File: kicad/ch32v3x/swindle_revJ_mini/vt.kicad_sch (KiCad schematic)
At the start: 8 parts, among them J2 Conn_01x03_Socket, U3 3V->VTREF, U4 VTREF->3V, U5 VTREF<->3V, U6 RT9013-33GB

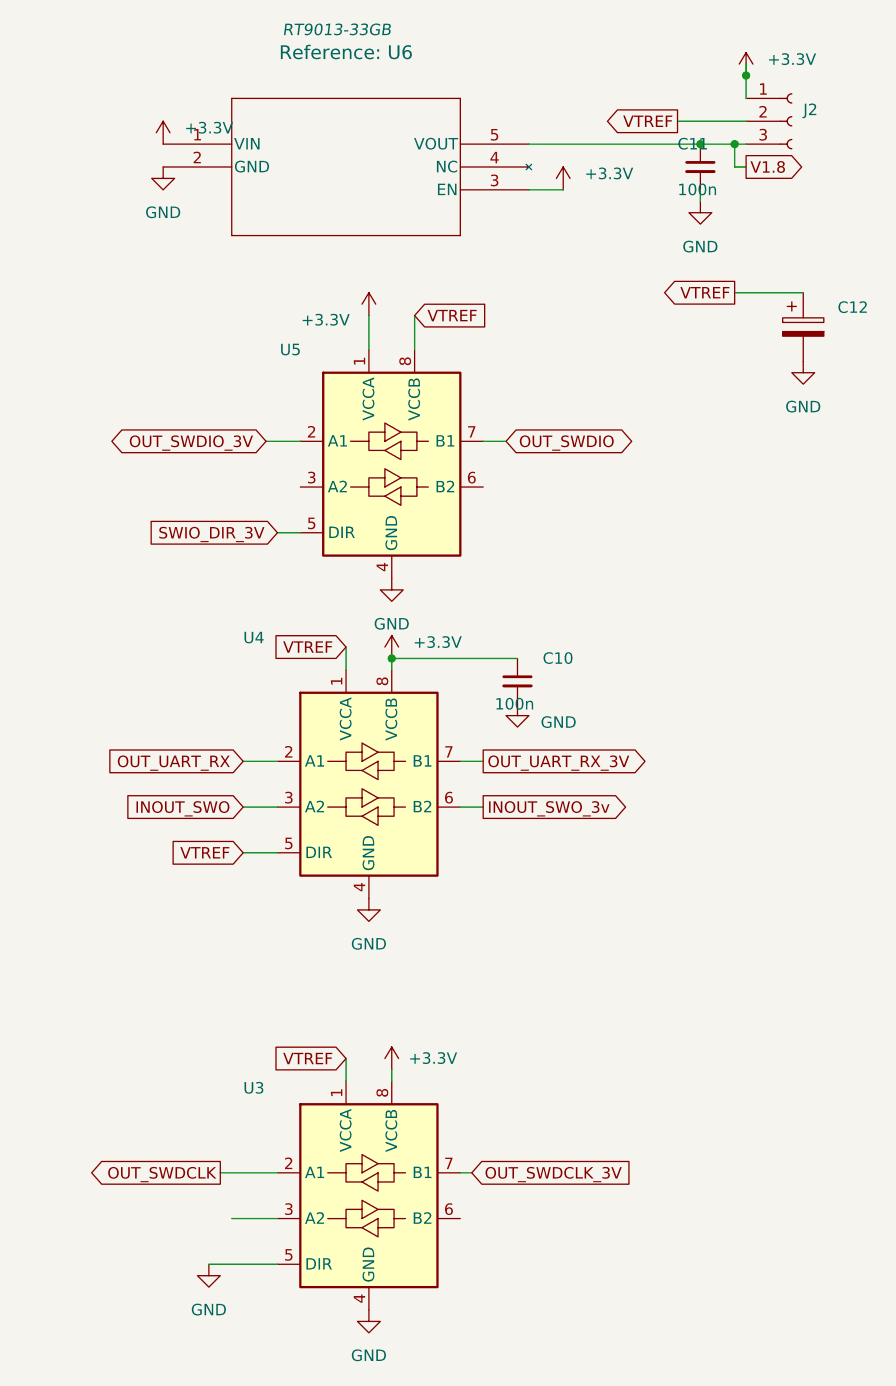
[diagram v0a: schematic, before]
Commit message: add a WS2812b to the mini version, mini version for CH32,GD32 and RP2xxx
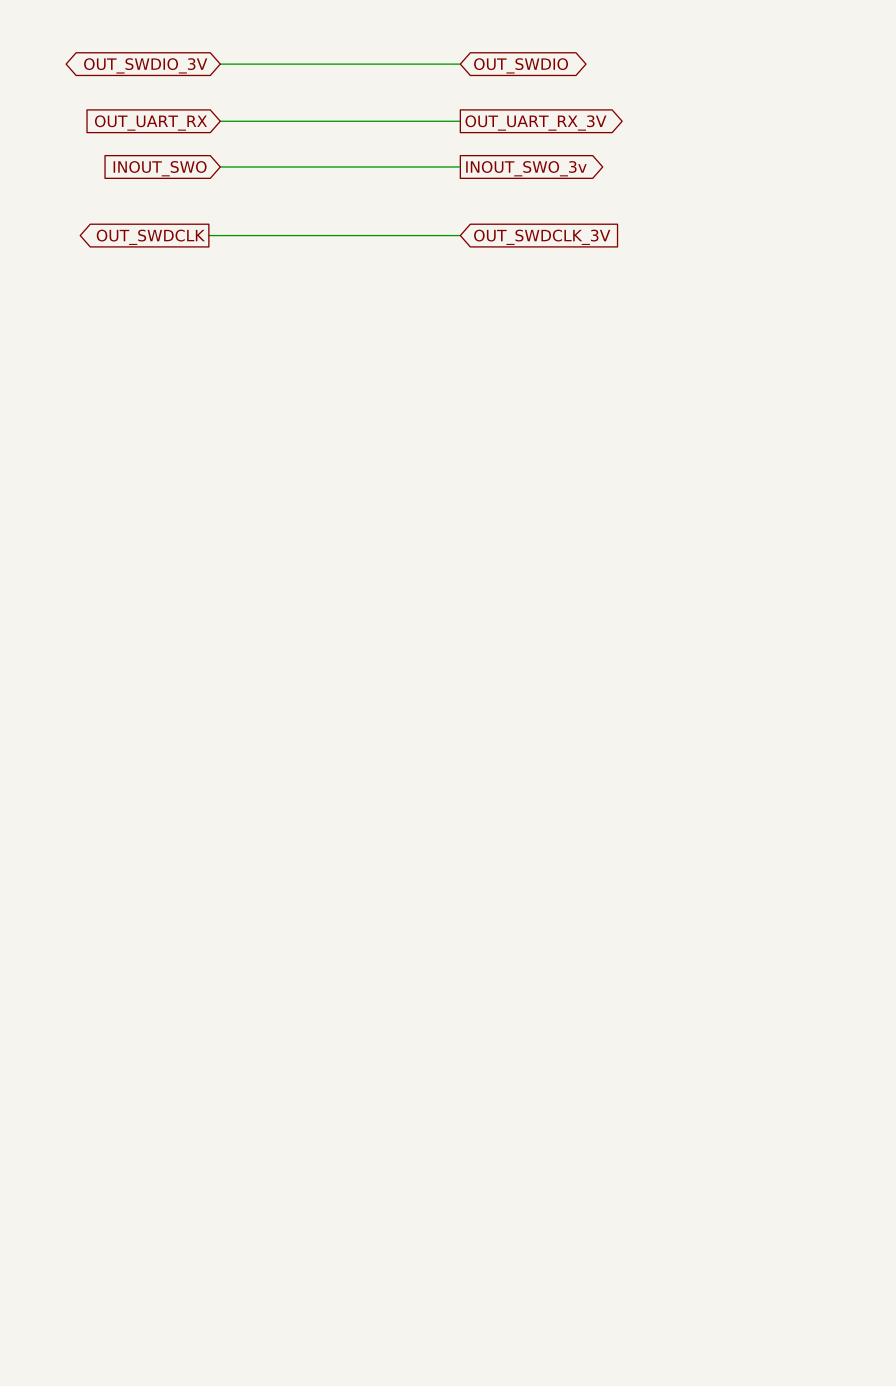
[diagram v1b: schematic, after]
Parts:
- removed C10, C11: 100n, Resistor_SMD:R_0603_1608Metric, symbol Device:C_Small
- removed C12: 100u, Capacitor_SMD:C_1206_3216Metric_Pad1.33x1.80mm_HandSolder, symbol Device:C_Polarized
- removed J2: Conn_01x03_Socket, Connector_PinHeader_2.54mm:PinHeader_1x03_P2.54mm_Vertical, symbol Connector:Conn_01x03_Socket
- removed U3: 3V->VTREF, Package_SO:TSSOP-8_3x3mm_P0.65mm, symbol Logic_LevelTranslator:SN74LVC2T45DCUR
- removed U4: VTREF->3V, Package_SO:TSSOP-8_3x3mm_P0.65mm, symbol Logic_LevelTranslator:SN74LVC2T45DCUR
- removed U5: VTREF<->3V, Package_SO:TSSOP-8_3x3mm_P0.65mm, symbol Logic_LevelTranslator:SN74LVC2T45DCUR
- removed U6: RT9013-33GB, PCM_Package_TO_SOT_SMD_AKL:TSOT-23-5, symbol 2024-10-20_09-04-45:RT9013-33GB

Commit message: kicad: order to pcbway
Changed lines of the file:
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@@
+	(wire
+		(pts
+			(xy 39.37 50.8) (xy 67.31 50.8)
+		)
+		(stroke
+			(width 0)
+			(type default)
+		)
+	)
 	(wire
 		(pts
@@
 		)
 	)
+	(global_label "INOUT_NRESET"
+		(shape bidirectional)
+		(at 67.31 50.8 0)
+		(fields_autoplaced yes)
+		(effects
+			(font
+				(size 1.27 1.27)
+			)
+			(justify left)
+		)
+		(property "Intersheetrefs" "${INTERSHEET_REFS}"
+			(at 83.3302 50.7206 0)
+			(effects
+				(font
+					(size 1.27 1.27)
+				)
+				(justify left)
+				(hide yes)
+			)
+		)
+	)
 	(global_label "OUT_UART_RX"
 		(shape input)
@@
 			(effects
 				(font
+					(size 1.27 1.27)
+				)
+				(justify right)
+				(hide yes)
+			)
+		)
+	)
+	(global_label "INOUT_NRESET_3V"
+		(shape bidirectional)
+		(at 39.37 50.8 180)
+		(fields_autoplaced yes)
+		(effects
+			(font
+				(size 1.27 1.27)
+			)
+			(justify right)
+		)
+		(property "Intersheetrefs" "${INTERSHEET_REFS}"
+			(at 18.4007 50.8 0)
+			(effects
+				(font
